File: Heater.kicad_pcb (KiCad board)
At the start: 2 copper layers, 100 x 100 mm, 89 parts, among them J1 OLED, J2 Conn_01x02_Socket, J3 Debug, J4 Conn_01x02_Pin, J5 Conn_01x02_Socket, Q1 2N7002, Q2 2N7002, Q3 2N7002, SW1 SW_MEC_5E, SW2 SW_MEC_5E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

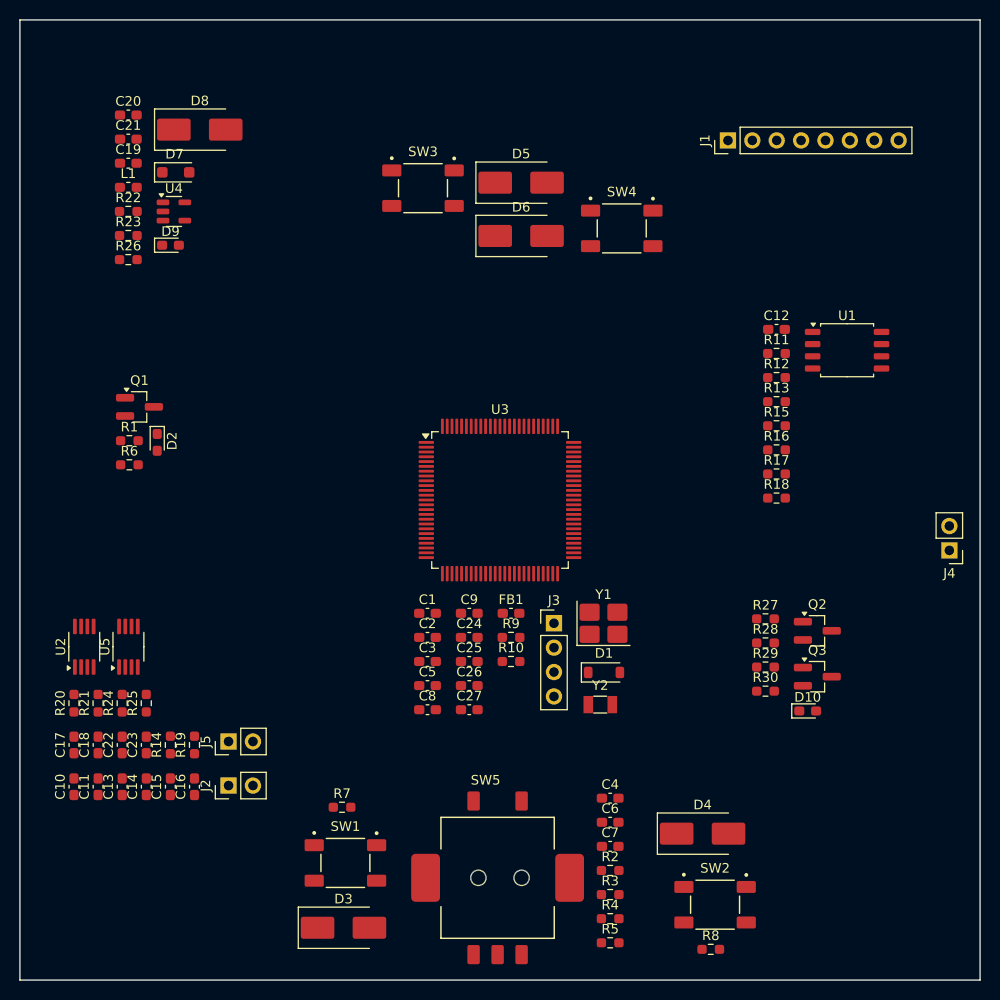
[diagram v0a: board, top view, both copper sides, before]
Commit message: feat: 完成了部分元件的layout
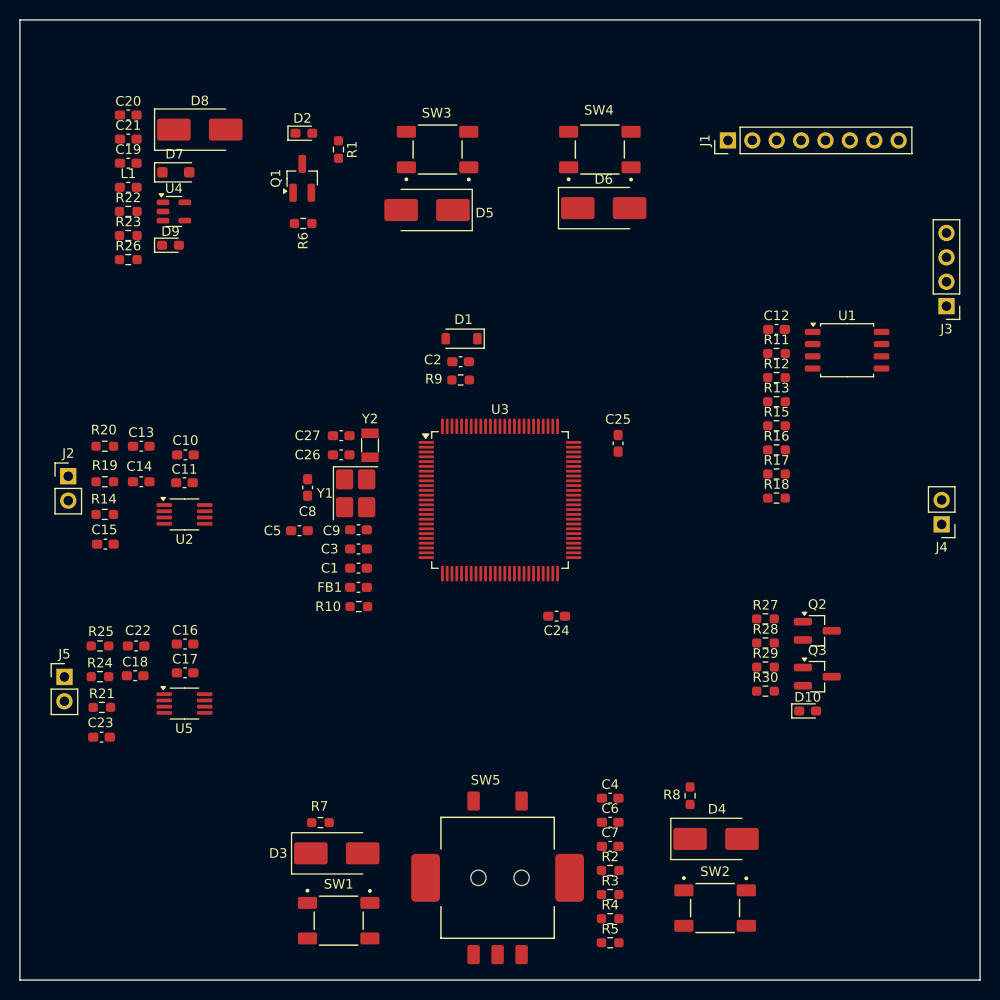
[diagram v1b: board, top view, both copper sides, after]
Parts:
- moved J3 52.6 mm to (96.5, -70.2), turned to 180 degrees
- moved D1 37.8 mm to (46.0, -66.8), turned to 180 degrees
- moved R1 37.3 mm to (33.2, -86.5), turned to -90 degrees
- moved C10 36.5 mm to (17.2, -54.7), turned to 0 degrees
- moved J2 36.3 mm to (5.04, -52.5), turned to 0 degrees
- moved Y2 36.1 mm to (36.5, -55.7), turned to -90 degrees
- moved D2 35.6 mm to (29.6, -88.2), turned to 0 degrees
- moved C13 35.5 mm to (12.6, -55.6), turned to 0 degrees
- moved C11 32.9 mm to (17.1, -51.8), turned to 0 degrees
- moved C14 31.8 mm to (12.6, -51.9), turned to 180 degrees
- moved C27 31.5 mm to (33.5, -56.7), turned to 180 degrees
- moved R6 31.0 mm to (29.5, -78.8), turned to 180 degrees
- moved Q1 29.2 mm to (29.4, -83.5), turned to 90 degrees
- moved Y1 29.2 mm to (35.0, -50.7), turned to -90 degrees
- moved R19 29.0 mm to (8.84, -51.9), turned to 0 degrees
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
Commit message: feat: 完成了PCB的layout，元件库存在部分修改
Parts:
- added +5V: PinHeader_1x02_P2.54mm_Vertical, Connector_PinHeader_2.54mm:PinHeader_1x02_P2.54mm_Vertical, F.Cu at (6.33, -90.1)
- added HEAT PWM: PinHeader_1x02_P2.54mm_Vertical, Connector_PinHeader_2.54mm:PinHeader_1x02_P2.54mm_Vertical, F.Cu at (96.0, -37.1)
- moved R5 32.2 mm to (33.7, -20.1), turned to -90 degrees
- moved R3 28.7 mm to (32.8, -9.40), turned to 180 degrees
- moved R4 27.6 mm to (37.5, -20.1), turned to -90 degrees
- moved C7 25.4 mm to (40.7, -28.6), turned to 180 degrees
- moved R2 25.1 mm to (36.6, -14.5), turned to 180 degrees
- moved C6 22.8 mm to (40.7, -25.8), turned to 180 degrees
- moved R27 22.5 mm to (92.4, -20.6), turned to 180 degrees
- moved J3 14.9 mm to (96.0, -55.3)
- moved R28 14.4 mm to (91.5, -39.0), turned to 90 degrees
- moved C21 13.2 mm to (18.8, -76.8)
- moved SW1 12.7 mm to (20.5, -6.80)
- moved R7 12.6 mm to (18.7, -17.7)
- moved D3 12.5 mm to (20.5, -13.8)
- moved D9 12.4 mm to (23.7, -86.0), turned to 180 degrees
- moved D8 12.0 mm to (23.9, -77.7), turned to -90 degrees
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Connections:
- SW5 pad : (no net) -> GND
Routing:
- net +3V3: track 0.00 -> 386.5 mm, vias 0 -> 9
- net +5V: track 0.00 -> 250.4 mm, vias 0 -> 2
- net /NRST: track 0.00 -> 92.4 mm
- net /PB4: track 0.00 -> 65.9 mm
- net /PD4: track 0.00 -> 61.0 mm
- net /PA6: track 0.00 -> 60.3 mm
- net /PD5: track 0.00 -> 57.8 mm
- net /PD6: track 0.00 -> 56.1 mm
- net /PD7: track 0.00 -> 54.9 mm
- net /PA8: track 0.00 -> 54.6 mm, vias 0 -> 2
- net /PB3: track 0.00 -> 53.9 mm
- net /PA9: track 0.00 -> 47.7 mm
- net /SWCLK: track 0.00 -> 46.2 mm, vias 0 -> 1
- net /PC7: track 0.00 -> 41.6 mm, vias 0 -> 2
- net /PC8: track 0.00 -> 41.4 mm, vias 0 -> 2
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- added copper zone on F.Cu, net /PC2
- added copper zone on F.Cu, net /PC3
- added copper zone on B.Cu, net GND
- added copper zone on F.Cu, net GND
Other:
- outline, holes or cut-outs redrawn
